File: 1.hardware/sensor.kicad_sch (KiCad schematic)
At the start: 11 parts, among them U22 Hall_Analog_Joystick

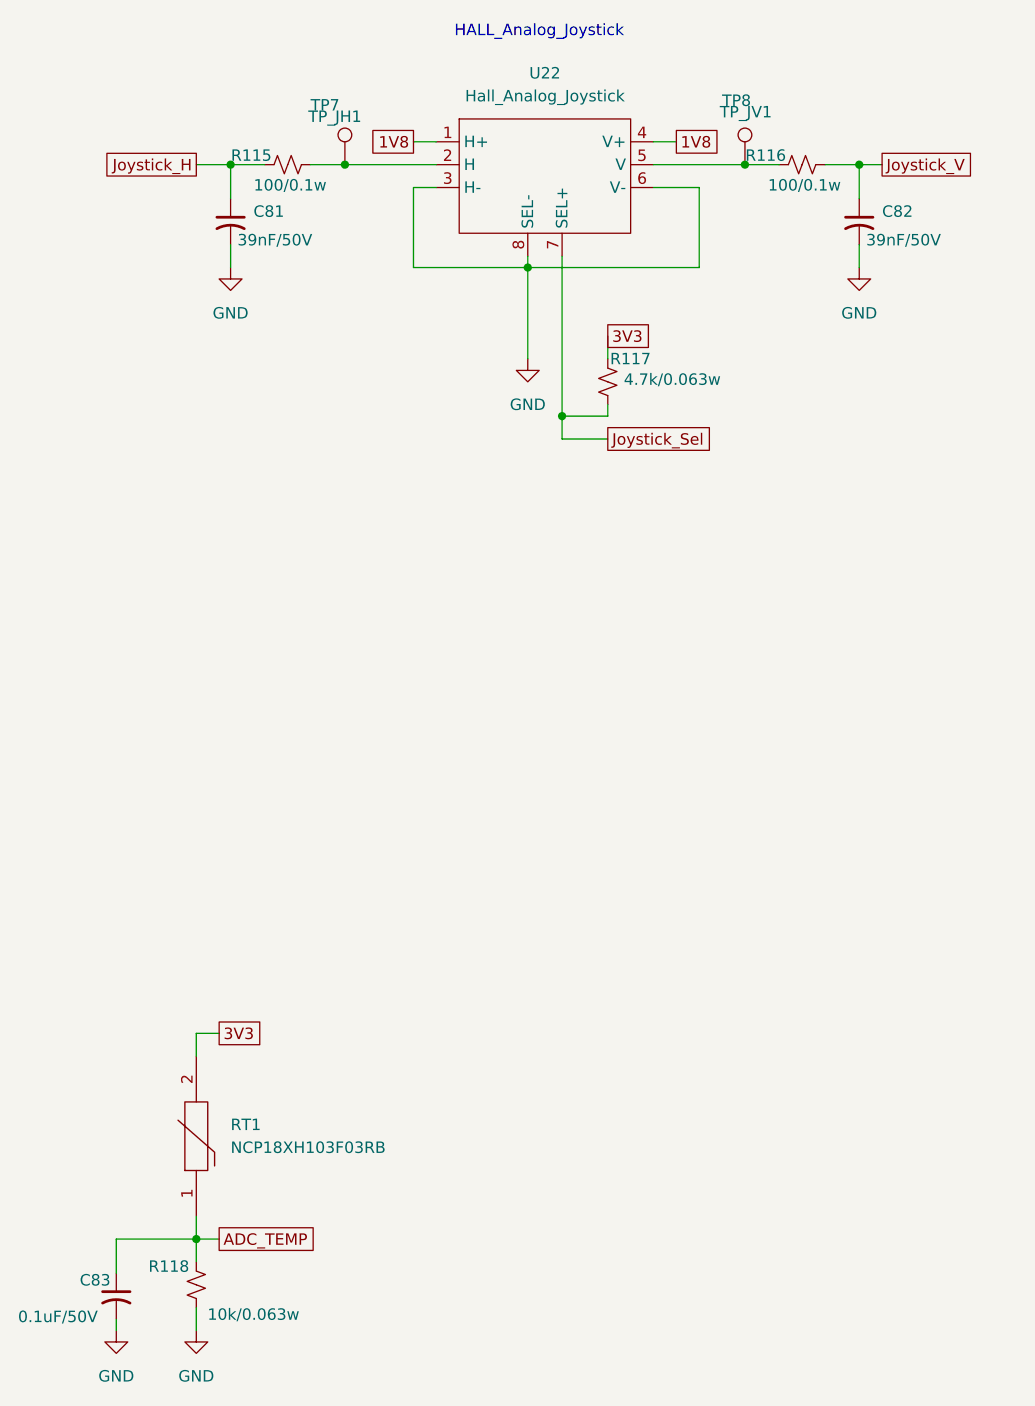
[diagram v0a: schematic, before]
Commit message: 부품 통일 및 필터 부분 캡 선정등 필요해보임
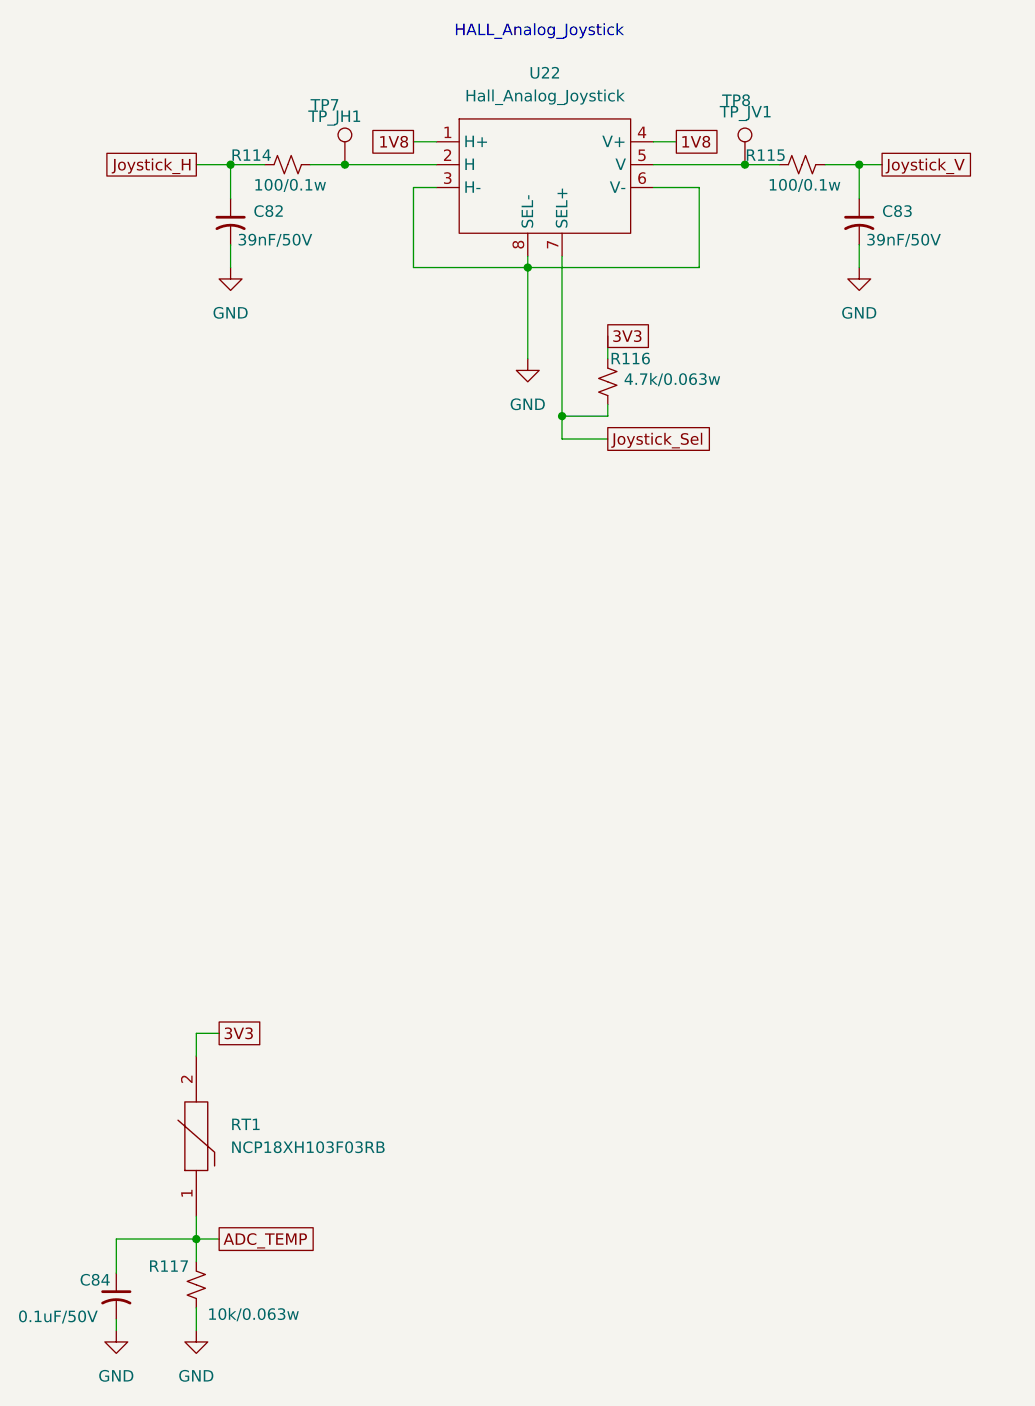
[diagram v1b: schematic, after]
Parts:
- TP7, TP8: now left out of the parts list
- renumbered C81 to C82, C82 to C83, C83 to C84, R115 to R114, R116 to R115, R117 to R116, R118 to R117
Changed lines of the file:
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@@
 		(dnp no)
 		(fields_autoplaced yes)
-		(property "Reference" "#PWR0115"
+		(property "Reference" "#PWR0111"
 			(at 93.98 100.33 0)
 			(effects
@@
 			(project "bldc_motor_controller"
 				(path "/a25adab6-a8c3-4e0e-8ba9-baac00aaa394/41a95291-f7f2-4bdf-b0a1-cf2084f10036"
-					(reference "#PWR0115")
+					(reference "#PWR0111")
 					(unit 1)
 				)
@@
 		(on_board yes)
 		(dnp no)
-		(property "Reference" "R118"
+		(property "Reference" "R117"
 			(at 54.102 194.818 0)
 			(effects
@@
 			(project "bldc_motor_controller"
 				(path "/a25adab6-a8c3-4e0e-8ba9-baac00aaa394/41a95291-f7f2-4bdf-b0a1-cf2084f10036"
-					(reference "R118")
+					(reference "R117")
 					(unit 1)
 				)
@@
 		(dnp no)
 		(fields_autoplaced yes)
-		(property "Reference" "#PWR0112"
+		(property "Reference" "#PWR0109"
 			(at 60.96 90.17 0)
 			(effects
@@
 			(project "bldc_motor_controller"
 				(path "/a25adab6-a8c3-4e0e-8ba9-baac00aaa394/41a95291-f7f2-4bdf-b0a1-cf2084f10036"
-					(reference "#PWR0112")
+					(reference "#PWR0109")
 					(unit 1)
 				)
@@
 		(on_board yes)
 		(dnp no)
-		(property "Reference" "R115"
+		(property "Reference" "R114"
 			(at 65.532 71.374 90)
 			(effects
@@
 			(project "bldc_motor_controller"
 				(path "/a25adab6-a8c3-4e0e-8ba9-baac00aaa394/41a95291-f7f2-4bdf-b0a1-cf2084f10036"
-					(reference "R115")
+					(reference "R114")
 					(unit 1)
 				)
@@
 		(dnp no)
 		(fields_autoplaced yes)
-		(property "Reference" "#PWR0116"
+		(property "Reference" "#PWR0112"
 			(at 48.26 208.28 0)
 			(effects
@@
 			(project "bldc_motor_controller"
 				(path "/a25adab6-a8c3-4e0e-8ba9-baac00aaa394/41a95291-f7f2-4bdf-b0a1-cf2084f10036"
-					(reference "#PWR0116")
+					(reference "#PWR0112")
 					(unit 1)
 				)
@@
 		(unit 1)
 		(exclude_from_sim no)
-		(in_bom yes)
+		(in_bom no)
 		(on_board yes)
 		(dnp no)
@@
 		(on_board yes)
 		(dnp no)
-		(property "Reference" "C81"
+		(property "Reference" "C82"
 			(at 63.5 77.5969 0)
 			(effects
@@
 			(project "bldc_motor_controller"
 				(path "/a25adab6-a8c3-4e0e-8ba9-baac00aaa394/41a95291-f7f2-4bdf-b0a1-cf2084f10036"
-					(reference "C81")
+					(reference "C82")
 					(unit 1)
 				)
@@
 		(dnp no)
 		(fields_autoplaced yes)
-		(property "Reference" "#PWR0117"
+		(property "Reference" "#PWR0113"
 			(at 57.15 208.28 0)
 			(effects
@@
 			(project "bldc_motor_controller"
 				(path "/a25adab6-a8c3-4e0e-8ba9-baac00aaa394/41a95291-f7f2-4bdf-b0a1-cf2084f10036"
-					(reference "#PWR0117")
+					(reference "#PWR0113")
 					(unit 1)
 				)
@@
 		(on_board yes)
 		(dnp no)
-		(property "Reference" "R117"
+		(property "Reference" "R116"
 			(at 103.124 93.98 0)
 			(effects
@@
 			(project "bldc_motor_controller"
 				(path "/a25adab6-a8c3-4e0e-8ba9-baac00aaa394/41a95291-f7f2-4bdf-b0a1-cf2084f10036"
-					(reference "R117")
+					(reference "R116")
 					(unit 1)
 				)
@@
 		(on_board yes)
 		(dnp no)
-		(property "Reference" "C83"
+		(property "Reference" "C84"
 			(at 44.196 196.342 0)
 			(effects
@@
 			(project "bldc_motor_controller"
 				(path "/a25adab6-a8c3-4e0e-8ba9-baac00aaa394/41a95291-f7f2-4bdf-b0a1-cf2084f10036"
-					(reference "C83")
+					(reference "C84")
 					(unit 1)
 				)
@@
 		(dnp no)
 		(fields_autoplaced yes)
-		(property "Reference" "#PWR0113"
+		(property "Reference" "#PWR0110"
 			(at 130.81 90.17 0)
 			(effects
@@
 			(project "bldc_motor_controller"
 				(path "/a25adab6-a8c3-4e0e-8ba9-baac00aaa394/41a95291-f7f2-4bdf-b0a1-cf2084f10036"
-					(reference "#PWR0113")
+					(reference "#PWR0110")
 					(unit 1)
 				)
@@
 		(unit 1)
 		(exclude_from_sim no)
-		(in_bom yes)
+		(in_bom no)
 		(on_board yes)
 		(dnp no)
@@
 		(on_board yes)
 		(dnp no)
-		(property "Reference" "C82"
+		(property "Reference" "C83"
 			(at 133.35 77.5969 0)
 			(effects
@@
 			(project "bldc_motor_controller"
 				(path "/a25adab6-a8c3-4e0e-8ba9-baac00aaa394/41a95291-f7f2-4bdf-b0a1-cf2084f10036"
-					(reference "C82")
+					(reference "C83")
 					(unit 1)
 				)
@@
 		(on_board yes)
 		(dnp no)
-		(property "Reference" "R116"
+		(property "Reference" "R115"
 			(at 122.682 71.374 90)
 			(effects
@@
 			(project "bldc_motor_controller"
 				(path "/a25adab6-a8c3-4e0e-8ba9-baac00aaa394/41a95291-f7f2-4bdf-b0a1-cf2084f10036"
-					(reference "R116")
-					(unit 1)
-				)
+					(reference "R115")
+					(unit 1)
+				)

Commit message: 거의 완성 근데 JLC에서 포지션이 좀 개판임
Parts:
- C82, C83: footprint Capacitor_SMD:C_0402_1005Metric -> Capacitor_SMD:C_0603_1608Metric
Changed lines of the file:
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@@
 			)
 		)
-		(property "Footprint" "Capacitor_SMD:C_0402_1005Metric"
+		(property "Footprint" "Capacitor_SMD:C_0603_1608Metric"
 			(at 60.96 78.74 0)
 			(effects
@@
 			)
 		)
-		(property "Footprint" "Capacitor_SMD:C_0402_1005Metric"
+		(property "Footprint" "Capacitor_SMD:C_0603_1608Metric"
 			(at 130.81 78.74 0)
 			(effects
